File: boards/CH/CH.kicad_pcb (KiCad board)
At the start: 2 copper layers, 23 parts, among them K1 NRP-02-C-05DH, K2 NRP-02-C-05DH, K3 NRP-02-C-05DH, K4 NRP-02-C-05DH, K5 HF49FD/005-1H11, U1 6N137, U2 6N137, U3 КР293КП2Б, X1 BH-12 (2×6), X2 B5B-XH-A, X3 DG301-5.0-02P, X4 B4B-XH-A, X5 DG301-5.0-02P

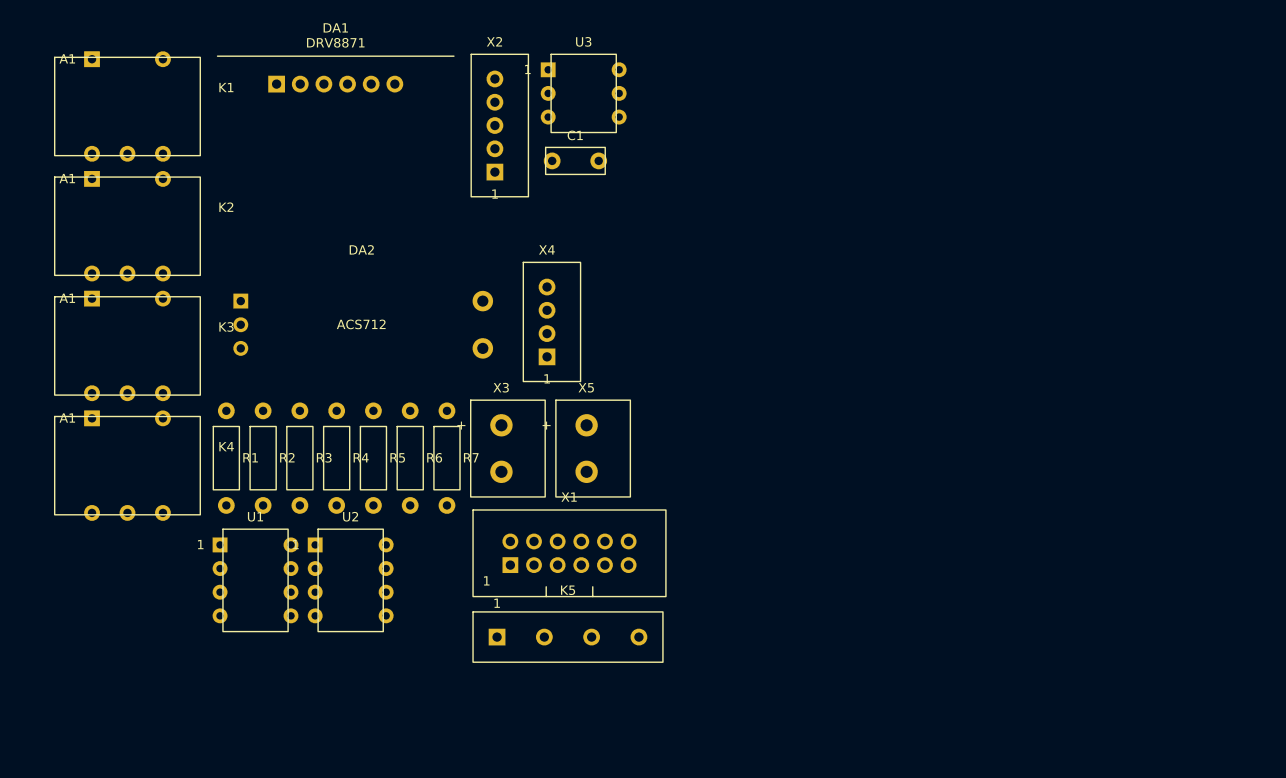
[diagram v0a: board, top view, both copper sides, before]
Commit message: Платы PS, MC, CH, LR: расстановка, трассировка, 3D-модели посадочных мест
PS:
- разведена по расстановке из файла: +24V_IN 6 мм (участок у K1 — 4 мм),
  шина +24V 6 мм с отводами 3 мм, +5P 2 мм, остров U2 1,5 мм;
  заливка GND_P на B.Cu, вырез заливки под островом, вырезы ⌀8 у крепежа
- классы цепей в PS.kicad_pro: Default, Power5, Power24, Island
- U1: посадочное место под модуль XL4015E 54 × 24 × 15 на штырях
  (пятаки IN/OUT, 2 стойки М3) по чертежу продавца; переразведены
  OUT+ и отвод +24V к IN+

MC:
- X5 перенесён, переразведены KH, +5P, GND_P в этой зоне
- FU1: место под Bourns MF-R110 (корпус 8,9 × 3,0 × 14,0)

CH:
- K1…K5, X5: места исправлены по datasheet (NRP-02, HF49FD, JST VH),
  переразведены цепи реле

LR:
- плата перекомпонована: X5…X8 — B5B-XH-A, как X1…X4; группы M1…M4
  по одному образцу (индикатор, разъём, защита в два ряда);
  X1…X4, X9 и DD1 на нижней стороне
- контур 176 × 59, 6 отверстий М3; разведена: сигналы F.Cu,
  GND_L заливкой B.Cu
- scripts/gen_LR_pcb.py удалён: описывал прежнюю раскладку с клеммами

Схемы:
- CH: X5 — JST VH (таблица Tbl_X5_CH_VH); MC: X3 — B4B-XH-A
  (кнопка KH с индикатором); PS: X11 убран; LR: у X5…X8 место
  B5B-XH-A
- sch_common: генератор не перезаписывает файл, сохранённый KiCad,
  без --force

3D-модели (lib/3dmodels):
- упрощённые по чертежам datasheet: NRP-02, HF49FD, NRP-15 (корпус),
  JST B2P-VH, Mornsun/K-CUT URB2405YMD (U2), Talema DPO-3.0-22 (кольцо
  лежит), Bourns MF-R110
- из библиотеки KiCad: PinSocket 1×3, 1×4, 1×12, Phoenix MKDS-1,5-2
- docs/3D-модели.md — источники размеров и что сверить

База компонентов: E-083 — Bourns MF-R110 (Ihold 1,1 А), «Выбран»;
csv перевыгружены
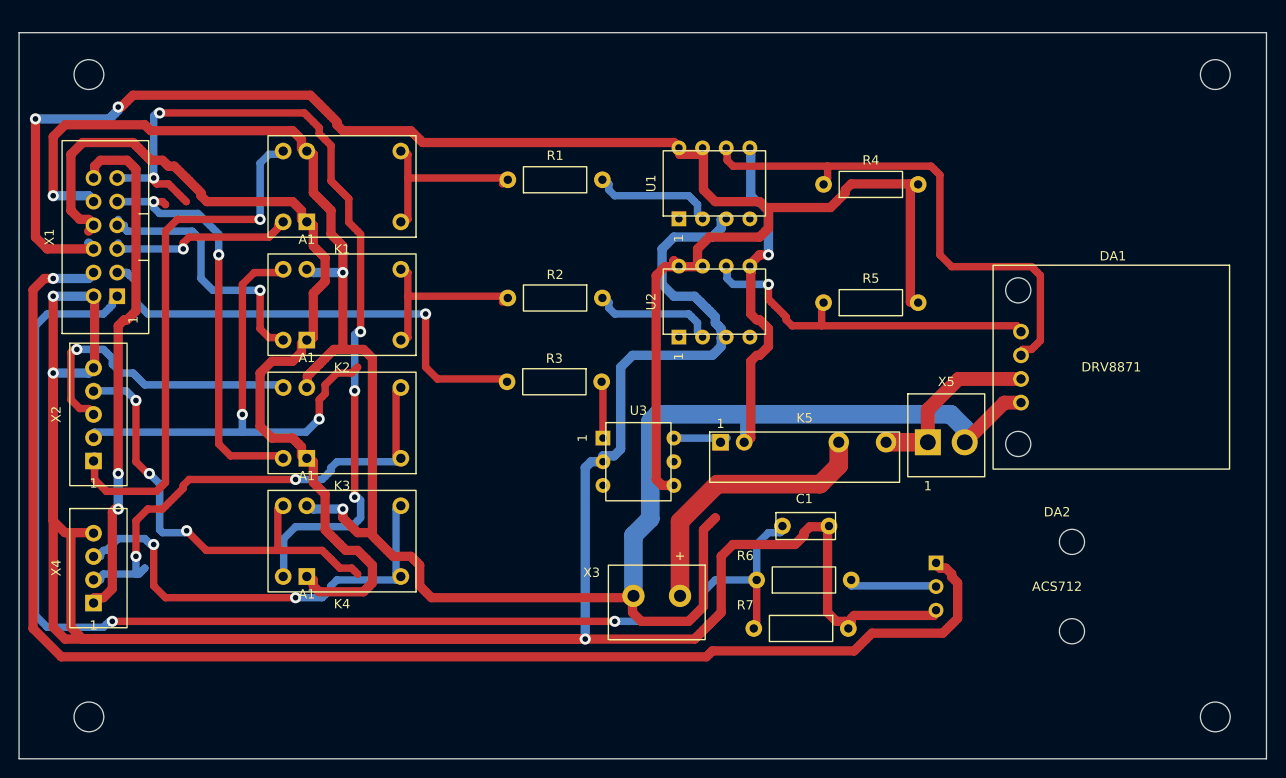
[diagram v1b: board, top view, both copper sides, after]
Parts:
- added H1: M3, manipulator:MountingHole_3.2mm_M3, F.Cu at (54.0, 43.5)
- added H2: M3, manipulator:MountingHole_3.2mm_M3, F.Cu at (175.0, 43.5)
- added H3: M3, manipulator:MountingHole_3.2mm_M3, F.Cu at (54.0, 112.5)
- added H4: M3, manipulator:MountingHole_3.2mm_M3, F.Cu at (175.0, 112.5)
- X5: value DG301-5.0-02P -> B2P-VH; footprint manipulator:TB_DG301-5.0_2P_V -> manipulator:JST_VH_B2P-VH
- moved DA1 88.7 mm to (163.8, 74.9), turned to -90 degrees
- moved DA2 79.8 mm to (158.0, 98.5)
- moved U1 65.2 mm to (121.2, 55.2), turned to 90 degrees
- moved R4 64.5 mm to (138.0, 55.3), turned to 90 degrees
- moved X1 60.3 mm to (55.8, 61.0), turned to 90 degrees
- moved R5 56.0 mm to (138.0, 68.0), turned to 90 degrees
- moved X4 55.4 mm to (54.5, 96.5)
- moved X2 53.1 mm to (54.5, 80.0)
- moved U2 49.2 mm to (121.2, 67.9), turned to 90 degrees
- moved C1 46.4 mm to (131.0, 92.0)
- moved R1 46.3 mm to (104.1, 54.8), turned to 90 degrees
- moved R6 44.3 mm to (130.8, 97.8), turned to 90 degrees
- moved R7 42.2 mm to (130.5, 103.0), turned to -90 degrees
- moved U3 40.0 mm to (113.0, 85.1)
- moved X5 38.6 mm to (146.1, 83.0)
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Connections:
- X5 pad 1: Net-(DA1-OUT1) -> +24V_M
- X5 pad 2: Net-(DA2-IP-) -> GND_P
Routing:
- net GND_L: track 0.00 -> 322.5 mm, vias 0 -> 3
- net GND_P: track 0.00 -> 261.8 mm, vias 0 -> 4
- net +5P: track 0.00 -> 185.8 mm, vias 0 -> 2
- net +5V_L: track 0.00 -> 153.2 mm, vias 0 -> 1
- net CURR: track 0.00 -> 135.4 mm, vias 0 -> 2
- net KH: track 0.00 -> 100.0 mm
- net Net-(K4-NC): track 0.00 -> 91.8 mm, vias 0 -> 5
- net IN1_LR: track 0.00 -> 57.8 mm, vias 0 -> 1
- net Net-(DA1-IN1): track 0.00 -> 57.2 mm
- net 3V3: track 0.00 -> 55.8 mm, vias 0 -> 2
- net IN2_LR: track 0.00 -> 54.4 mm, vias 0 -> 2
- net RELE: track 0.00 -> 52.1 mm, vias 0 -> 1
- net Net-(K3-COM): track 0.00 -> 51.7 mm, vias 0 -> 2
- net SCL_LR: track 0.00 -> 48.6 mm, vias 0 -> 3
- net Net-(K4-COM): track 0.00 -> 48.5 mm, vias 0 -> 2
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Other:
- board outline added: 134 x 78 mm
